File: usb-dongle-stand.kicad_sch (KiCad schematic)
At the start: 15 parts, among them J1 TYPE-C-31-M-12, P1 YTC-TC16S-128

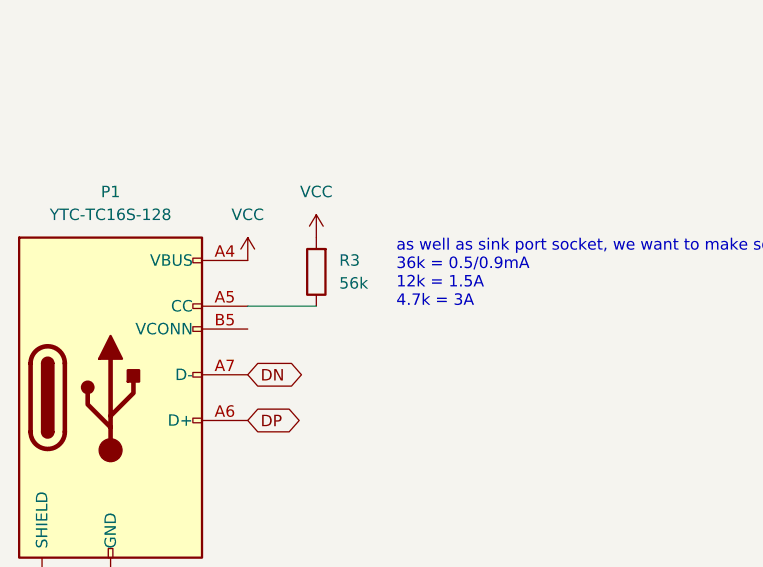
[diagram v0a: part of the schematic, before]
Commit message: correct DFP CC resistor
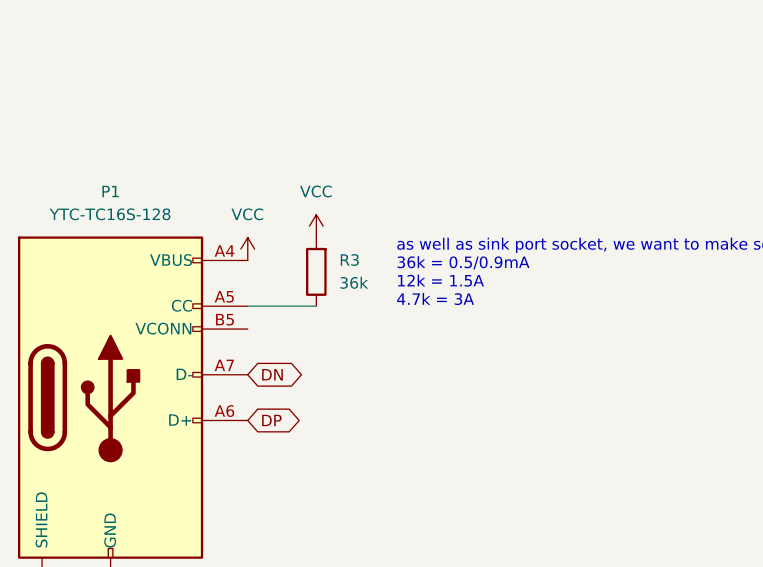
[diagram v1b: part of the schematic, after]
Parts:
- R3: value 56k -> 36k
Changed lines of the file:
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@@
 			)
 		)
-		(property "Value" "56k"
+		(property "Value" "36k"
 			(at 60.96 119.3799 0)
 			(effects
